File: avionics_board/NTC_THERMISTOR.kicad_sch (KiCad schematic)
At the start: 2 parts

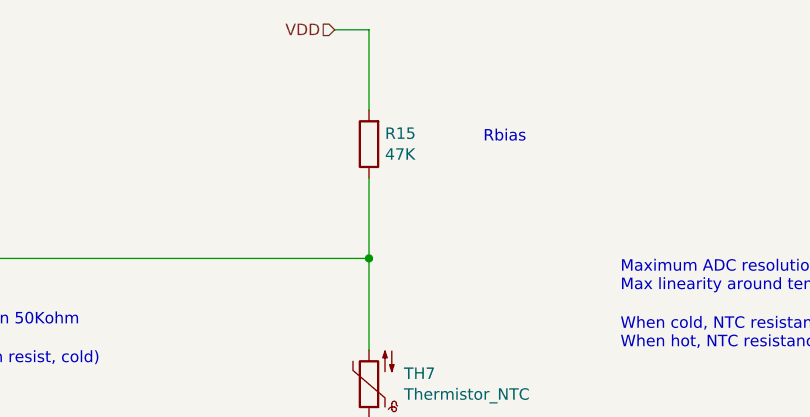
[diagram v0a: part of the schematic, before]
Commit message: use SAMTEC connectors for AVI to side panels, try HARWIN ones next
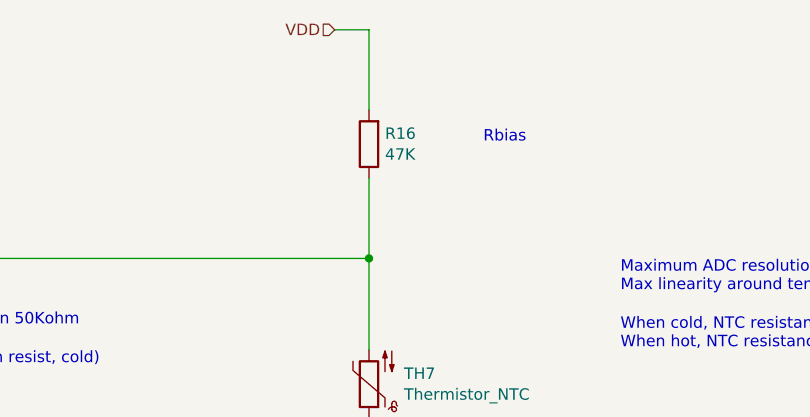
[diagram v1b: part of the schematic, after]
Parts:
- renumbered R15 to R16
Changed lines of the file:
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@@
 		(on_board yes)
 		(dnp no)
-		(property "Reference" "R15"
+		(property "Reference" "R16"
 			(at 122.428 47.0916 0)
 			(effects
@@
 			(project "AVIONICS_BOARD"
 				(path "/f6cc00ab-17f1-4973-862f-7ac95fe70668/4b32b6cb-e4ab-41a8-b61c-93e0ce1b94ae/00000000-0000-0000-0000-00005eb419ee"
+					(reference "R16")
+					(unit 1)
+				)
+				(path "/f6cc00ab-17f1-4973-862f-7ac95fe70668/4b32b6cb-e4ab-41a8-b61c-93e0ce1b94ae/00000000-0000-0000-0000-00005ec0237f"
+					(reference "R17")
+					(unit 1)
+				)
+				(path "/f6cc00ab-17f1-4973-862f-7ac95fe70668/4b32b6cb-e4ab-41a8-b61c-93e0ce1b94ae/00000000-0000-0000-0000-00005ec02646"
+					(reference "R10")
+					(unit 1)
+				)
+				(path "/f6cc00ab-17f1-4973-862f-7ac95fe70668/4b32b6cb-e4ab-41a8-b61c-93e0ce1b94ae/00000000-0000-0000-0000-00005ec0264b"
+					(reference "R11")
+					(unit 1)
+				)
+				(path "/f6cc00ab-17f1-4973-862f-7ac95fe70668/4b32b6cb-e4ab-41a8-b61c-93e0ce1b94ae/00000000-0000-0000-0000-00005ec02e34"
+					(reference "R13")
+					(unit 1)
+				)
+				(path "/f6cc00ab-17f1-4973-862f-7ac95fe70668/4b32b6cb-e4ab-41a8-b61c-93e0ce1b94ae/00000000-0000-0000-0000-00005ec02e39"
+					(reference "R14")
+					(unit 1)
+				)
+				(path "/f6cc00ab-17f1-4973-862f-7ac95fe70668/4b32b6cb-e4ab-41a8-b61c-93e0ce1b94ae/00000000-0000-0000-0000-00005ec02e3e"
 					(reference "R15")
 					(unit 1)
 				)
-				(path "/f6cc00ab-17f1-4973-862f-7ac95fe70668/4b32b6cb-e4ab-41a8-b61c-93e0ce1b94ae/00000000-0000-0000-0000-00005ec0237f"
-					(reference "R16")
-					(unit 1)
-				)
-				(path "/f6cc00ab-17f1-4973-862f-7ac95fe70668/4b32b6cb-e4ab-41a8-b61c-93e0ce1b94ae/00000000-0000-0000-0000-00005ec02646"
-					(reference "R9")
-					(unit 1)
-				)
-				(path "/f6cc00ab-17f1-4973-862f-7ac95fe70668/4b32b6cb-e4ab-41a8-b61c-93e0ce1b94ae/00000000-0000-0000-0000-00005ec0264b"
-					(reference "R10")
-					(unit 1)
-				)
-				(path "/f6cc00ab-17f1-4973-862f-7ac95fe70668/4b32b6cb-e4ab-41a8-b61c-93e0ce1b94ae/00000000-0000-0000-0000-00005ec02e34"
+				(path "/f6cc00ab-17f1-4973-862f-7ac95fe70668/4b32b6cb-e4ab-41a8-b61c-93e0ce1b94ae/00000000-0000-0000-0000-00005ec02e43"
 					(reference "R12")
 					(unit 1)
 				)
-				(path "/f6cc00ab-17f1-4973-862f-7ac95fe70668/4b32b6cb-e4ab-41a8-b61c-93e0ce1b94ae/00000000-0000-0000-0000-00005ec02e39"
-					(reference "R13")
-					(unit 1)
-				)
-				(path "/f6cc00ab-17f1-4973-862f-7ac95fe70668/4b32b6cb-e4ab-41a8-b61c-93e0ce1b94ae/00000000-0000-0000-0000-00005ec02e3e"
-					(reference "R14")
-					(unit 1)
-				)
-				(path "/f6cc00ab-17f1-4973-862f-7ac95fe70668/4b32b6cb-e4ab-41a8-b61c-93e0ce1b94ae/00000000-0000-0000-0000-00005ec02e43"
-					(reference "R11")
-					(unit 1)
-				)

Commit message: AVI: using through hole M50 connectors for sun detectors and ACS
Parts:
- R16: Order https://www.digikey.com/product-detail/en/bourns-inc/CR0603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 -> (none)
- TH7: Order https://www.digikey.com/product-detail/en/murata-electronic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 -> (none)
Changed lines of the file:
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@@
-			)
-		)
-		(property "Order" "https://www.digikey.com/product-detail/en/murata-electronics/NXFT15WB473FA2B150/490-14853-ND/6606459"
-			(at 120.65 74.93 90)
-			(effects
-				(font
-					(size 1.27 1.27)
-				)
-				(hide yes)
 			)
 		)
@@
 			(at 120.65 48.26 0)
 			(effects
-				(font
-					(size 1.27 1.27)
-				)
-				(hide yes)
-			)
-		)
-		(property "Order" "https://www.digikey.com/product-detail/en/bourns-inc/CR0603-FX-4702ELF/CR0603-FX-4702ELFCT-ND/3925317"
-			(at 120.65 48.26 0)
-			(effects

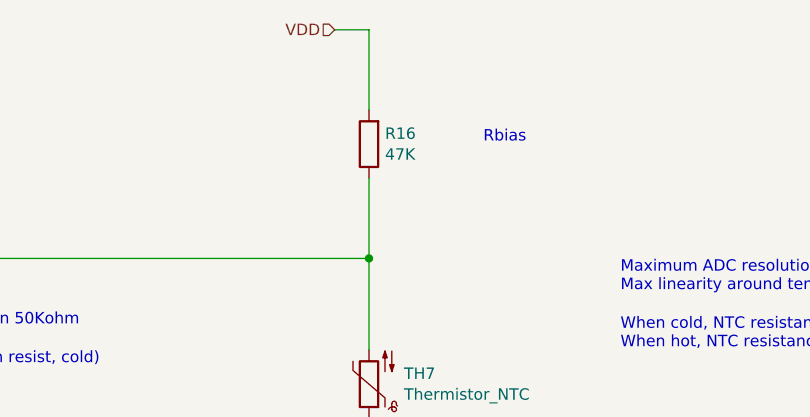
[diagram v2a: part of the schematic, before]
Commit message: QC, add second 3V regulator to AUX, INT pullups on AUX SCI AVI
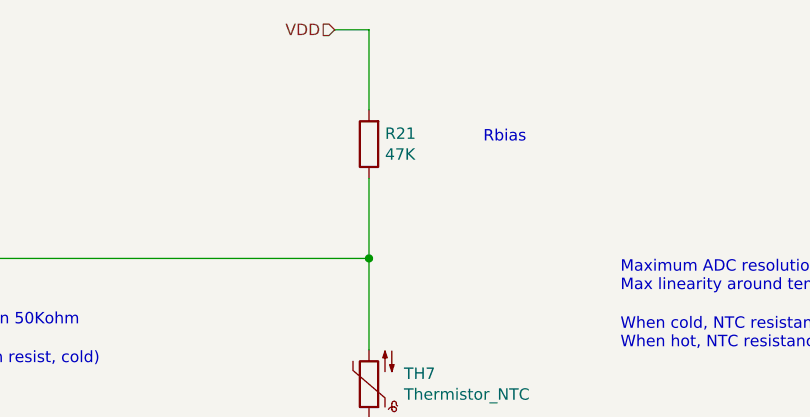
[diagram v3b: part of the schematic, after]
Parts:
- renumbered R16 to R21
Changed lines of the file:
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@@
 		(on_board yes)
 		(dnp no)
-		(property "Reference" "R16"
+		(property "Reference" "R21"
 			(at 122.428 47.0916 0)
 			(effects
@@
 			(project "AVIONICS_BOARD"
 				(path "/f6cc00ab-17f1-4973-862f-7ac95fe70668/4b32b6cb-e4ab-41a8-b61c-93e0ce1b94ae/00000000-0000-0000-0000-00005eb419ee"
+					(reference "R21")
+					(unit 1)
+				)
+				(path "/f6cc00ab-17f1-4973-862f-7ac95fe70668/4b32b6cb-e4ab-41a8-b61c-93e0ce1b94ae/00000000-0000-0000-0000-00005ec0237f"
+					(reference "R22")
+					(unit 1)
+				)
+				(path "/f6cc00ab-17f1-4973-862f-7ac95fe70668/4b32b6cb-e4ab-41a8-b61c-93e0ce1b94ae/00000000-0000-0000-0000-00005ec02646"
+					(reference "R15")
+					(unit 1)
+				)
+				(path "/f6cc00ab-17f1-4973-862f-7ac95fe70668/4b32b6cb-e4ab-41a8-b61c-93e0ce1b94ae/00000000-0000-0000-0000-00005ec0264b"
 					(reference "R16")
 					(unit 1)
 				)
-				(path "/f6cc00ab-17f1-4973-862f-7ac95fe70668/4b32b6cb-e4ab-41a8-b61c-93e0ce1b94ae/00000000-0000-0000-0000-00005ec0237f"
+				(path "/f6cc00ab-17f1-4973-862f-7ac95fe70668/4b32b6cb-e4ab-41a8-b61c-93e0ce1b94ae/00000000-0000-0000-0000-00005ec02e34"
+					(reference "R18")
+					(unit 1)
+				)
+				(path "/f6cc00ab-17f1-4973-862f-7ac95fe70668/4b32b6cb-e4ab-41a8-b61c-93e0ce1b94ae/00000000-0000-0000-0000-00005ec02e39"
+					(reference "R19")
+					(unit 1)
+				)
+				(path "/f6cc00ab-17f1-4973-862f-7ac95fe70668/4b32b6cb-e4ab-41a8-b61c-93e0ce1b94ae/00000000-0000-0000-0000-00005ec02e3e"
+					(reference "R20")
+					(unit 1)
+				)
+				(path "/f6cc00ab-17f1-4973-862f-7ac95fe70668/4b32b6cb-e4ab-41a8-b61c-93e0ce1b94ae/00000000-0000-0000-0000-00005ec02e43"
 					(reference "R17")
 					(unit 1)
 				)
-				(path "/f6cc00ab-17f1-4973-862f-7ac95fe70668/4b32b6cb-e4ab-41a8-b61c-93e0ce1b94ae/00000000-0000-0000-0000-00005ec02646"
-					(reference "R10")
-					(unit 1)
-				)
-				(path "/f6cc00ab-17f1-4973-862f-7ac95fe70668/4b32b6cb-e4ab-41a8-b61c-93e0ce1b94ae/00000000-0000-0000-0000-00005ec0264b"
-					(reference "R11")
-					(unit 1)
-				)
-				(path "/f6cc00ab-17f1-4973-862f-7ac95fe70668/4b32b6cb-e4ab-41a8-b61c-93e0ce1b94ae/00000000-0000-0000-0000-00005ec02e34"
-					(reference "R13")
-					(unit 1)
-				)
-				(path "/f6cc00ab-17f1-4973-862f-7ac95fe70668/4b32b6cb-e4ab-41a8-b61c-93e0ce1b94ae/00000000-0000-0000-0000-00005ec02e39"
-					(reference "R14")
-					(unit 1)
-				)
-				(path "/f6cc00ab-17f1-4973-862f-7ac95fe70668/4b32b6cb-e4ab-41a8-b61c-93e0ce1b94ae/00000000-0000-0000-0000-00005ec02e3e"
-					(reference "R15")
-					(unit 1)
-				)
-				(path "/f6cc00ab-17f1-4973-862f-7ac95fe70668/4b32b6cb-e4ab-41a8-b61c-93e0ce1b94ae/00000000-0000-0000-0000-00005ec02e43"
-					(reference "R12")
-					(unit 1)
-				)

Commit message: AVI board manages its local powers
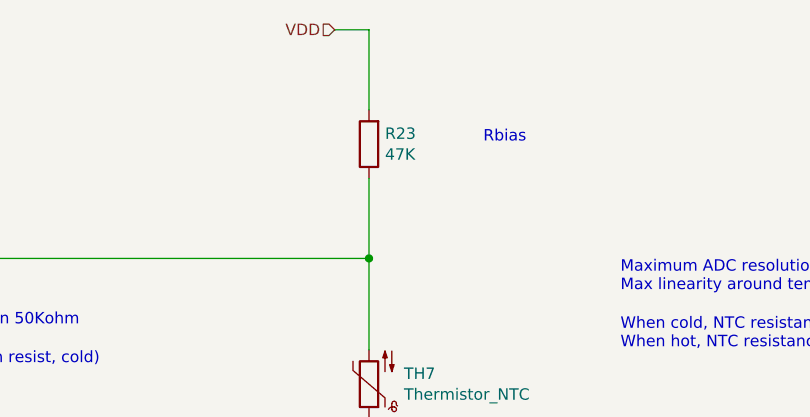
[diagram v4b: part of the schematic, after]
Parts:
- renumbered R21 to R23
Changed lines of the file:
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@@
 		(on_board yes)
 		(dnp no)
-		(property "Reference" "R21"
+		(property "Reference" "R23"
 			(at 122.428 47.0916 0)
 			(effects
@@
 			(project "AVIONICS_BOARD"
 				(path "/f6cc00ab-17f1-4973-862f-7ac95fe70668/4b32b6cb-e4ab-41a8-b61c-93e0ce1b94ae/00000000-0000-0000-0000-00005eb419ee"
+					(reference "R23")
+					(unit 1)
+				)
+				(path "/f6cc00ab-17f1-4973-862f-7ac95fe70668/4b32b6cb-e4ab-41a8-b61c-93e0ce1b94ae/00000000-0000-0000-0000-00005ec0237f"
+					(reference "R24")
+					(unit 1)
+				)
+				(path "/f6cc00ab-17f1-4973-862f-7ac95fe70668/4b32b6cb-e4ab-41a8-b61c-93e0ce1b94ae/00000000-0000-0000-0000-00005ec02646"
+					(reference "R17")
+					(unit 1)
+				)
+				(path "/f6cc00ab-17f1-4973-862f-7ac95fe70668/4b32b6cb-e4ab-41a8-b61c-93e0ce1b94ae/00000000-0000-0000-0000-00005ec0264b"
+					(reference "R18")
+					(unit 1)
+				)
+				(path "/f6cc00ab-17f1-4973-862f-7ac95fe70668/4b32b6cb-e4ab-41a8-b61c-93e0ce1b94ae/00000000-0000-0000-0000-00005ec02e34"
+					(reference "R20")
+					(unit 1)
+				)
+				(path "/f6cc00ab-17f1-4973-862f-7ac95fe70668/4b32b6cb-e4ab-41a8-b61c-93e0ce1b94ae/00000000-0000-0000-0000-00005ec02e39"
 					(reference "R21")
 					(unit 1)
 				)
-				(path "/f6cc00ab-17f1-4973-862f-7ac95fe70668/4b32b6cb-e4ab-41a8-b61c-93e0ce1b94ae/00000000-0000-0000-0000-00005ec0237f"
+				(path "/f6cc00ab-17f1-4973-862f-7ac95fe70668/4b32b6cb-e4ab-41a8-b61c-93e0ce1b94ae/00000000-0000-0000-0000-00005ec02e3e"
 					(reference "R22")
 					(unit 1)
 				)
-				(path "/f6cc00ab-17f1-4973-862f-7ac95fe70668/4b32b6cb-e4ab-41a8-b61c-93e0ce1b94ae/00000000-0000-0000-0000-00005ec02646"
-					(reference "R15")
-					(unit 1)
-				)
-				(path "/f6cc00ab-17f1-4973-862f-7ac95fe70668/4b32b6cb-e4ab-41a8-b61c-93e0ce1b94ae/00000000-0000-0000-0000-00005ec0264b"
-					(reference "R16")
-					(unit 1)
-				)
-				(path "/f6cc00ab-17f1-4973-862f-7ac95fe70668/4b32b6cb-e4ab-41a8-b61c-93e0ce1b94ae/00000000-0000-0000-0000-00005ec02e34"
-					(reference "R18")
-					(unit 1)
-				)
-				(path "/f6cc00ab-17f1-4973-862f-7ac95fe70668/4b32b6cb-e4ab-41a8-b61c-93e0ce1b94ae/00000000-0000-0000-0000-00005ec02e39"
+				(path "/f6cc00ab-17f1-4973-862f-7ac95fe70668/4b32b6cb-e4ab-41a8-b61c-93e0ce1b94ae/00000000-0000-0000-0000-00005ec02e43"
 					(reference "R19")
 					(unit 1)
 				)
-				(path "/f6cc00ab-17f1-4973-862f-7ac95fe70668/4b32b6cb-e4ab-41a8-b61c-93e0ce1b94ae/00000000-0000-0000-0000-00005ec02e3e"
-					(reference "R20")
-					(unit 1)
-				)
-				(path "/f6cc00ab-17f1-4973-862f-7ac95fe70668/4b32b6cb-e4ab-41a8-b61c-93e0ce1b94ae/00000000-0000-0000-0000-00005ec02e43"
-					(reference "R17")
-					(unit 1)
-				)
